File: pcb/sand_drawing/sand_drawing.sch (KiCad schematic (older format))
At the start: 31 parts, among them J0 12V GND, J1 Stepper1, J2 Stepper2, J3 Opto 1, J4 Opto 2, J5 UART, J6 ESP POWER, U2 AMS1117-3.3, U3 ESP32-WROOM-32D

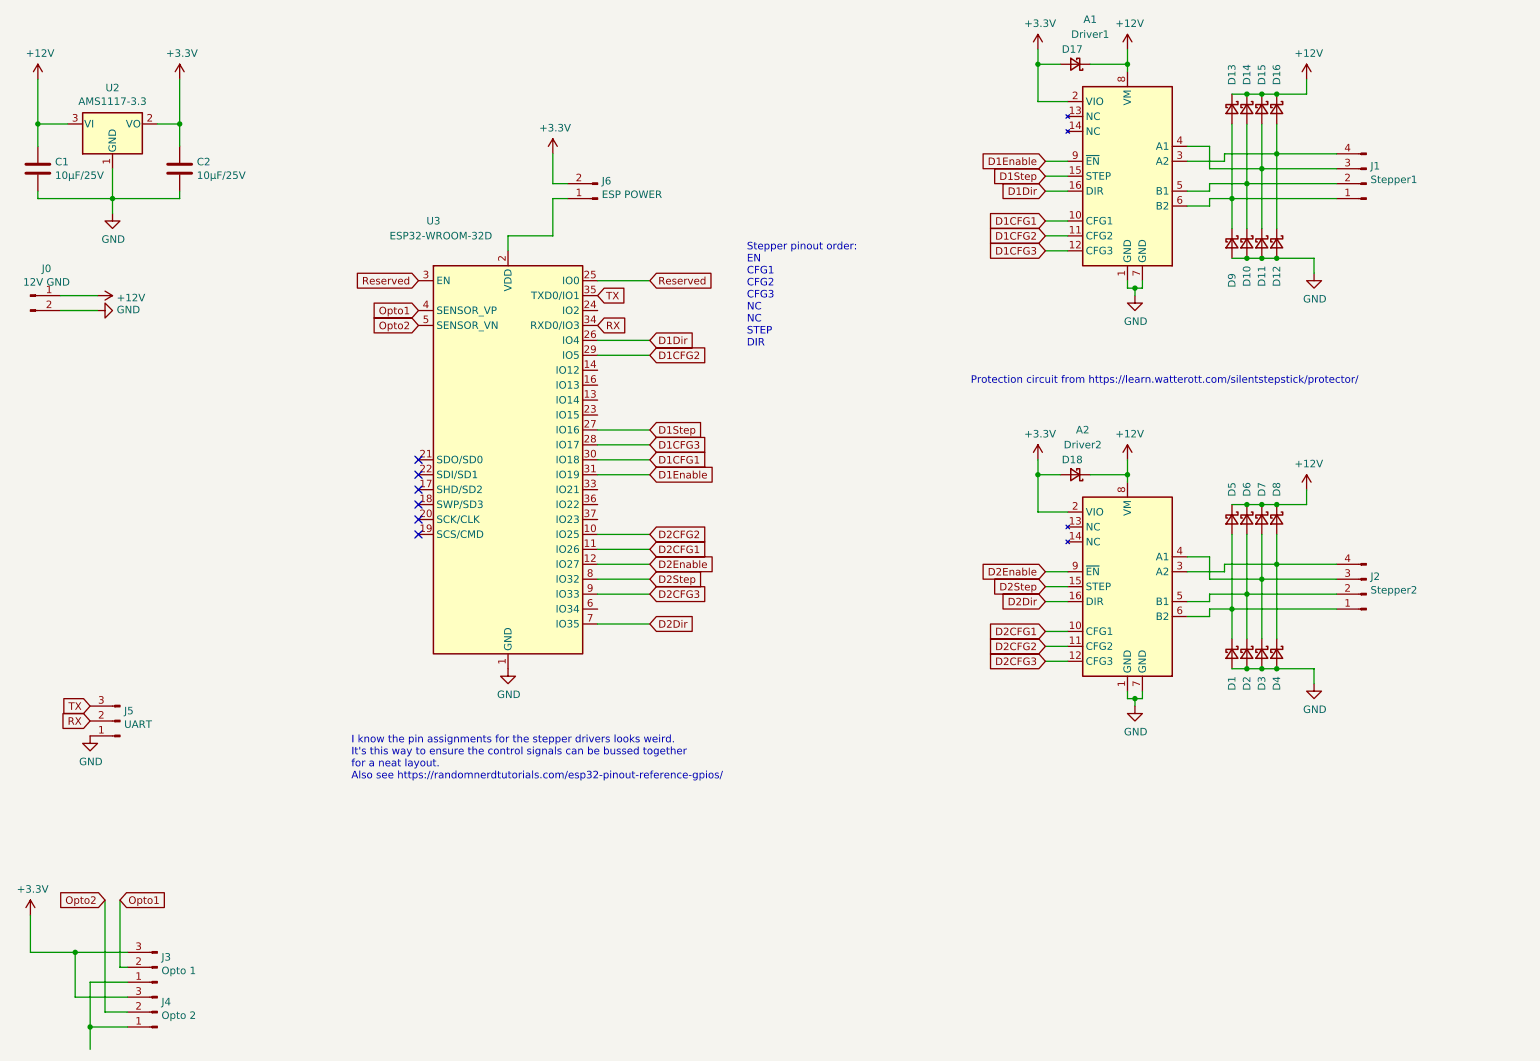
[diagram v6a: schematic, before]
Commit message: Finished hooking up the EN and IO0 buttons.
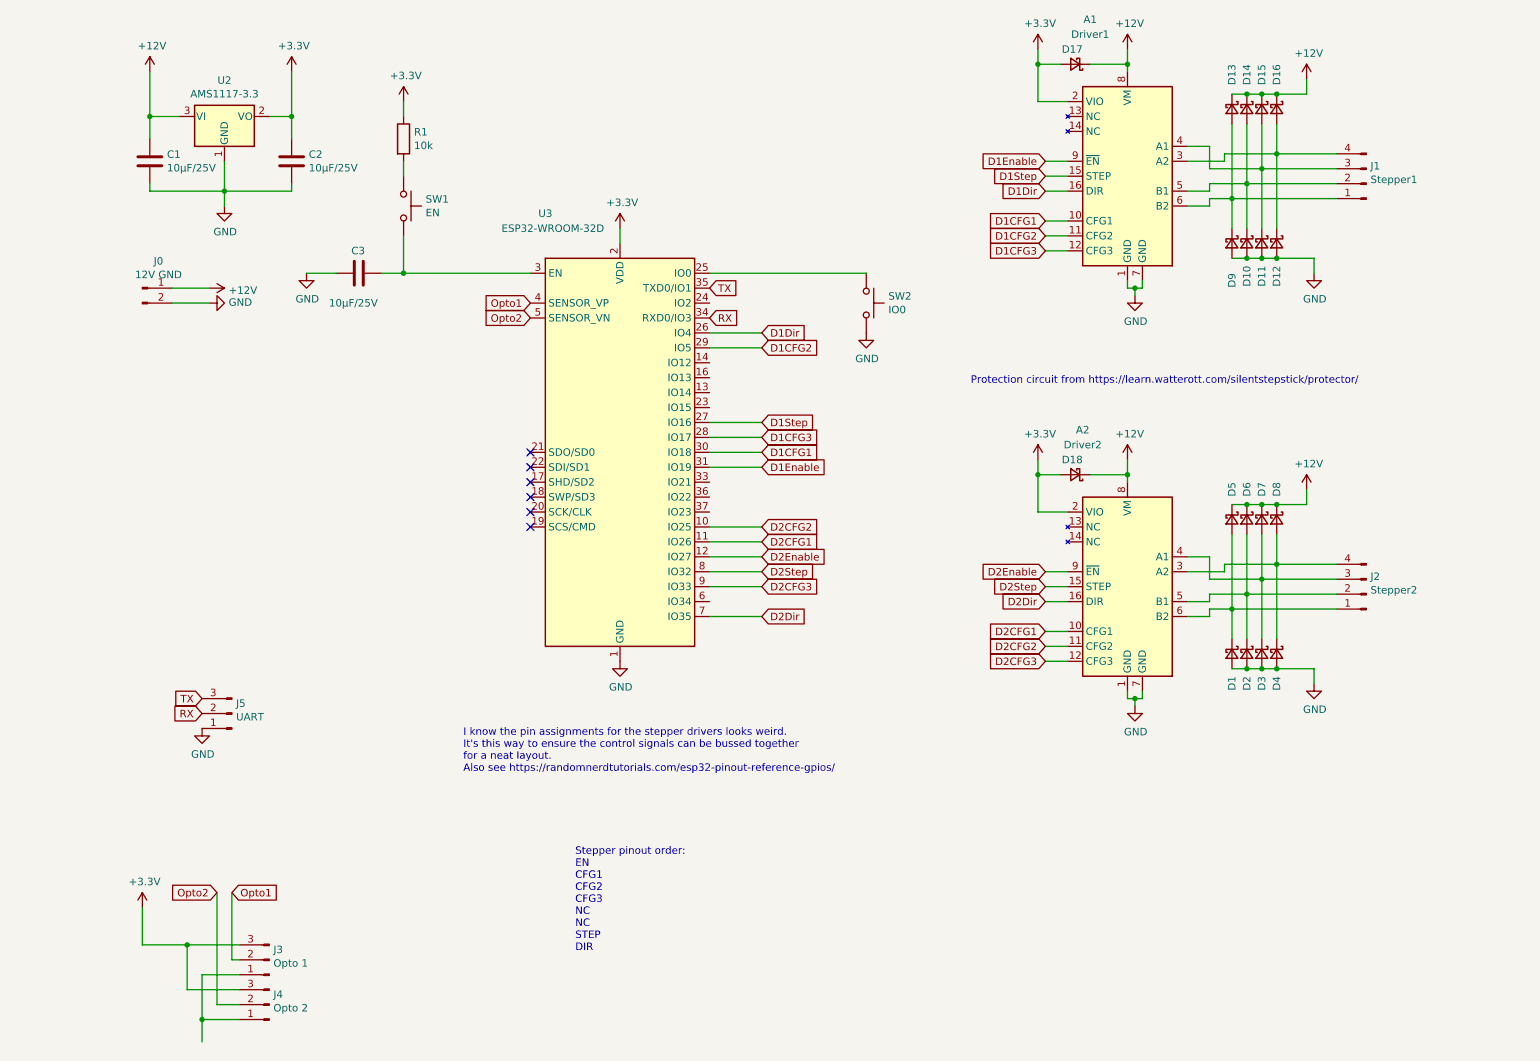
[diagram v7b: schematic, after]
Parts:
- removed J6: ESP POWER, Socket_Strips:Socket_Strip_Straight_1x02_Pitch2.54mm, symbol Connector:Conn_01x02_Male
- added C3: 10µF/25V, Capacitors_SMD:C_0805, symbol Device:C
- added R1: 10k, Capacitors_SMD:C_0603, symbol Device:R
- added SW1: EN, Buttons_Switches_THT:SW_PUSH_6mm, symbol Switch:SW_Push
- added SW2: IO0, Buttons_Switches_THT:SW_PUSH_6mm, symbol Switch:SW_Push
- C1, C2: footprint Capacitor_SMD:C_0805_2012Metric -> Capacitors_SMD:C_0805
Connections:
- net +3V3: now also U3.2 (VDD), R1.1
- net GND: now also C3.2, SW2.2
- net Reserved: no longer names the net of U3.25 (IO0)
- net Reserved: now also SW2.1; no longer U3.3 (EN)
- new net: C3.1, SW1.2, U3.3 (EN)
- new net: R1.2, SW1.1
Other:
- moved on the sheet: C1, C2, J0, J3, J4, J5, U2, U3
